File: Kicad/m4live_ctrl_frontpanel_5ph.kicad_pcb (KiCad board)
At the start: 4 copper layers, 25 x 128.5 mm, 0 parts

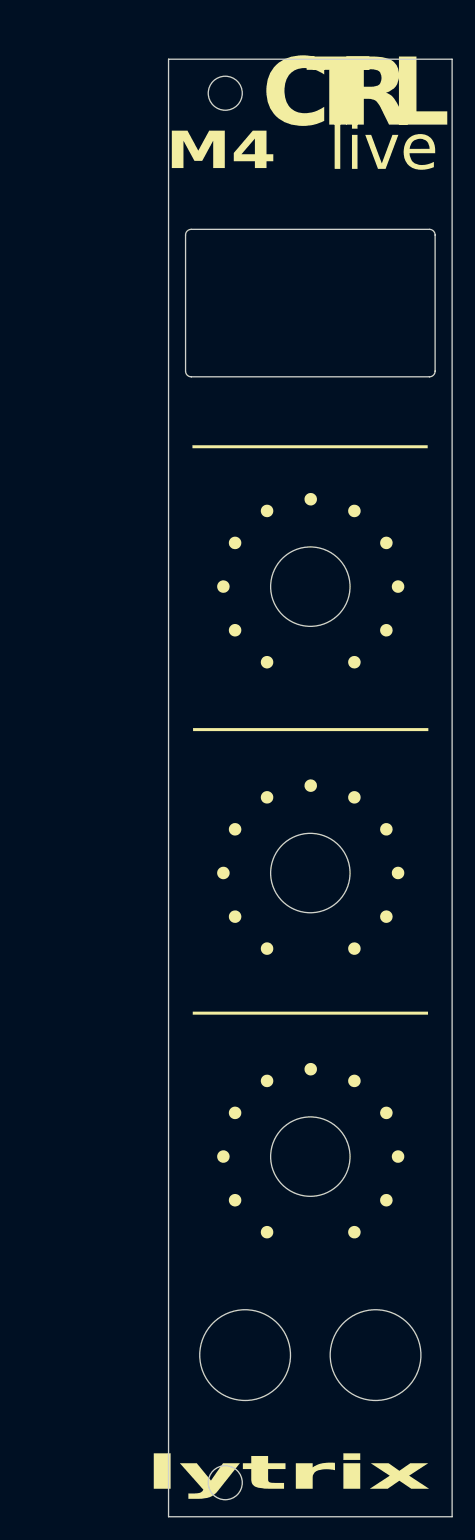
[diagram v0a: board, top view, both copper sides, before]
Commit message: Added temp supports for screen opening to prevent crack during manufacturing
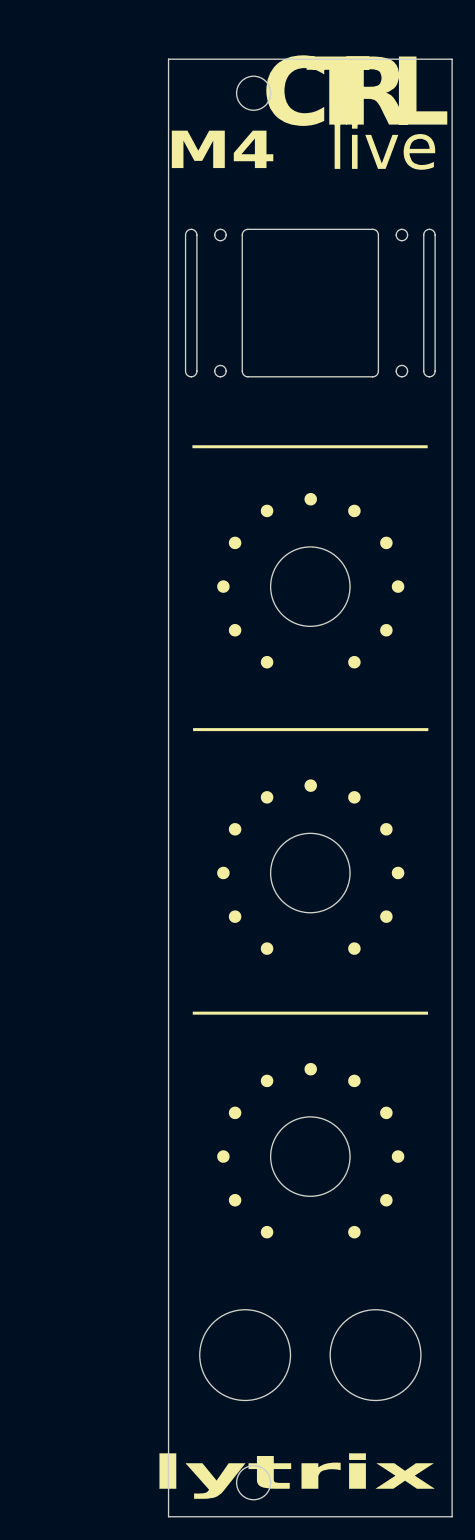
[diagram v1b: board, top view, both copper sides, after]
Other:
- outline, holes or cut-outs redrawn
- copper layers 4 -> 2
